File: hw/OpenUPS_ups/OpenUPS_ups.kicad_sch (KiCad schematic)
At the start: 1 part

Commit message: More cleanups and stuff
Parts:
- removed U?: ATtiny204-SS, Package_SO:SOIC-14_3.9x8.7mm_P1.27mm, symbol MCU_Microchip_ATtiny:ATtiny204-SS
- added C706 (x2): 100n 10V, Capacitor_SMD:C_0603_1608Metric, symbol Device:C_Small
- added U101: AVR32DB28x-xSO, Package_SO:SOIC-28W_7.5x17.9mm_P1.27mm, symbol MCU_Microchip_AVR_Dx:AVR32DB28x-xSO
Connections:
- net GND: now also C706.2, C706.2, U101.15 (AGND), U101.21 (GND)
- new net +3V3: C706.1, C706.1, U101.14 (AVDD), U101.20 (VDD), U101.6 (VDDIO2)
- new net I2C_E_SCL: U101.5 (PC3)
- new net I2C_E_SDA: U101.4 (PC2)
- new net I2C_I_SCL: U101.25 (PA3)
- new net I2C_I_SDA: U101.24 (PA2)
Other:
- added sheet Adj_Buck_Boost (12V_Buck_Boost.kicad_sch)
- sheet 12V Buck_Boost ports: added CLIND, CS1, CS2, EN, INT, SCL, SDA, Vin, Vout; removed none
- sheet 5V Buck ports: added EN; removed none
- note added: "Battery terminal goes here"
- note added: "Compatible with any 28-pin SOIC DA, DB or DD device"
- note added: "I2C Ma SCL"
- note added: "I2C Ma SDA"
- note added: "I2C Sl SCL"
- note added: "I2C Sl SDA"

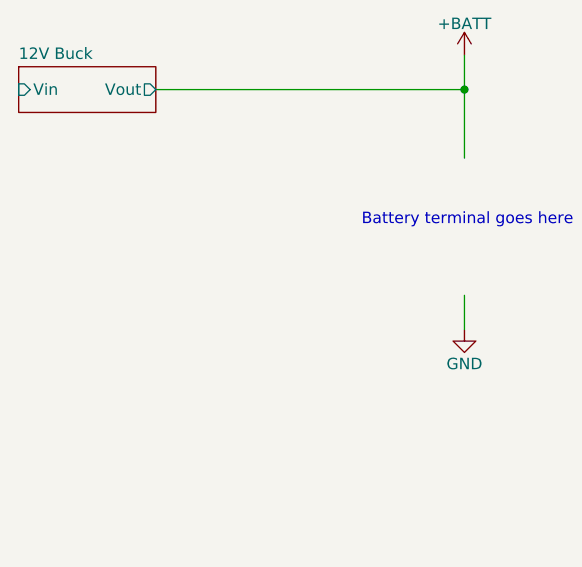
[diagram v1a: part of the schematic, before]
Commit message: Preliminary battery charger circuit
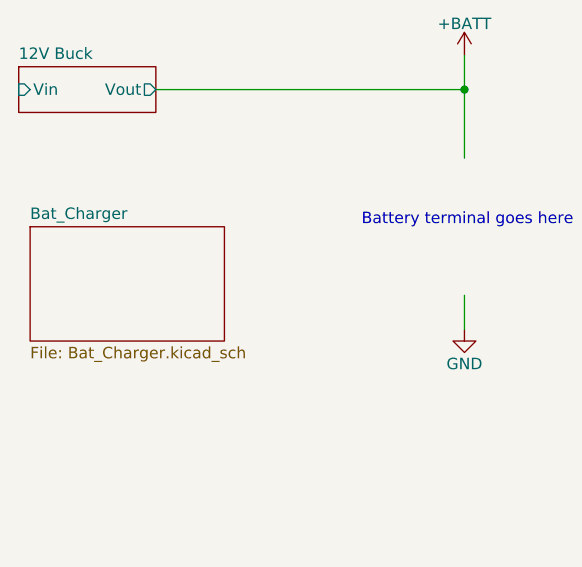
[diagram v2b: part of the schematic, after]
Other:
- added sheet Bat_Charger (Bat_Charger.kicad_sch)
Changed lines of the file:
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@@
+    )
+  )
+  (sheet (at 52.07 62.23) (size 21.59 12.7) (fields_autoplaced)
+    (stroke (width 0.1524) (type solid))
+    (fill (color 0 0 0 0.0000))
+    (property "Sheetname" "Bat_Charger" (at 52.07 61.5184 0)
+      (effects (font (size 1.27 1.27)) (justify left bottom))
+    )
+    (property "Sheetfile" "Bat_Charger.kicad_sch" (at 52.07 75.5146 0)
+      (effects (font (size 1.27 1.27)) (justify left top))
+    )
+    (instances
+      (project "OpenUPS_ups"
+        (path "/f77faec3-eac4-47f3-a2de-ec4a039f4502" (page "6"))
+      )
     )
   )

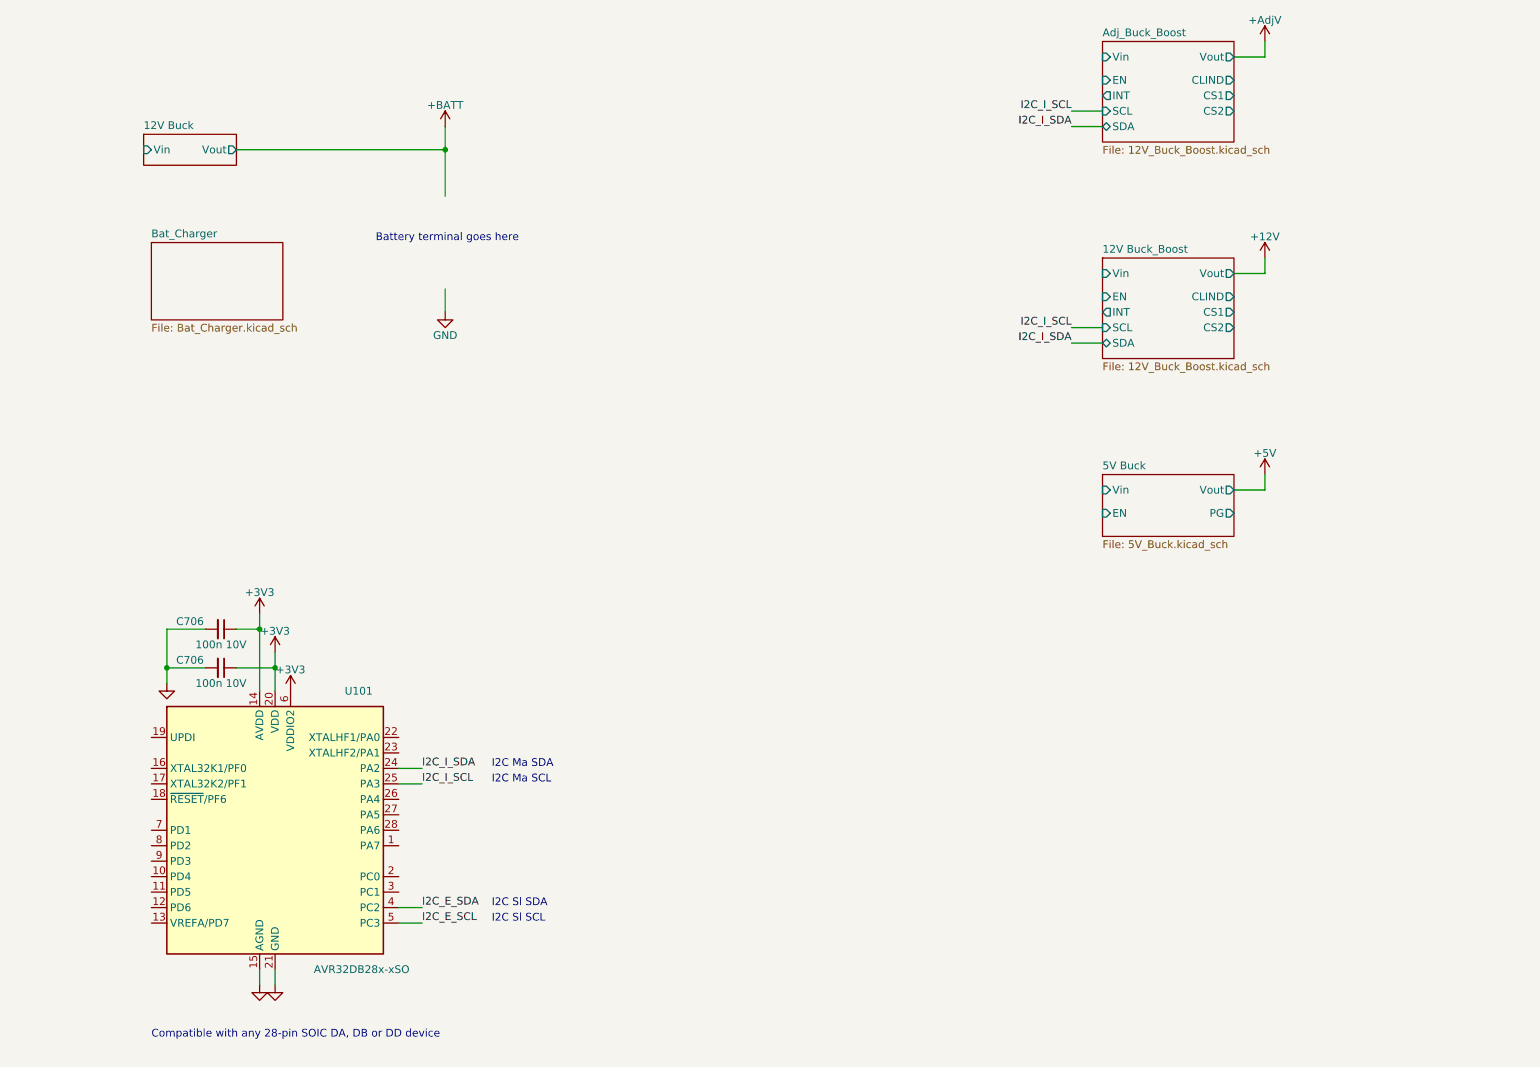
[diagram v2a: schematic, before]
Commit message: Secondary blocks design
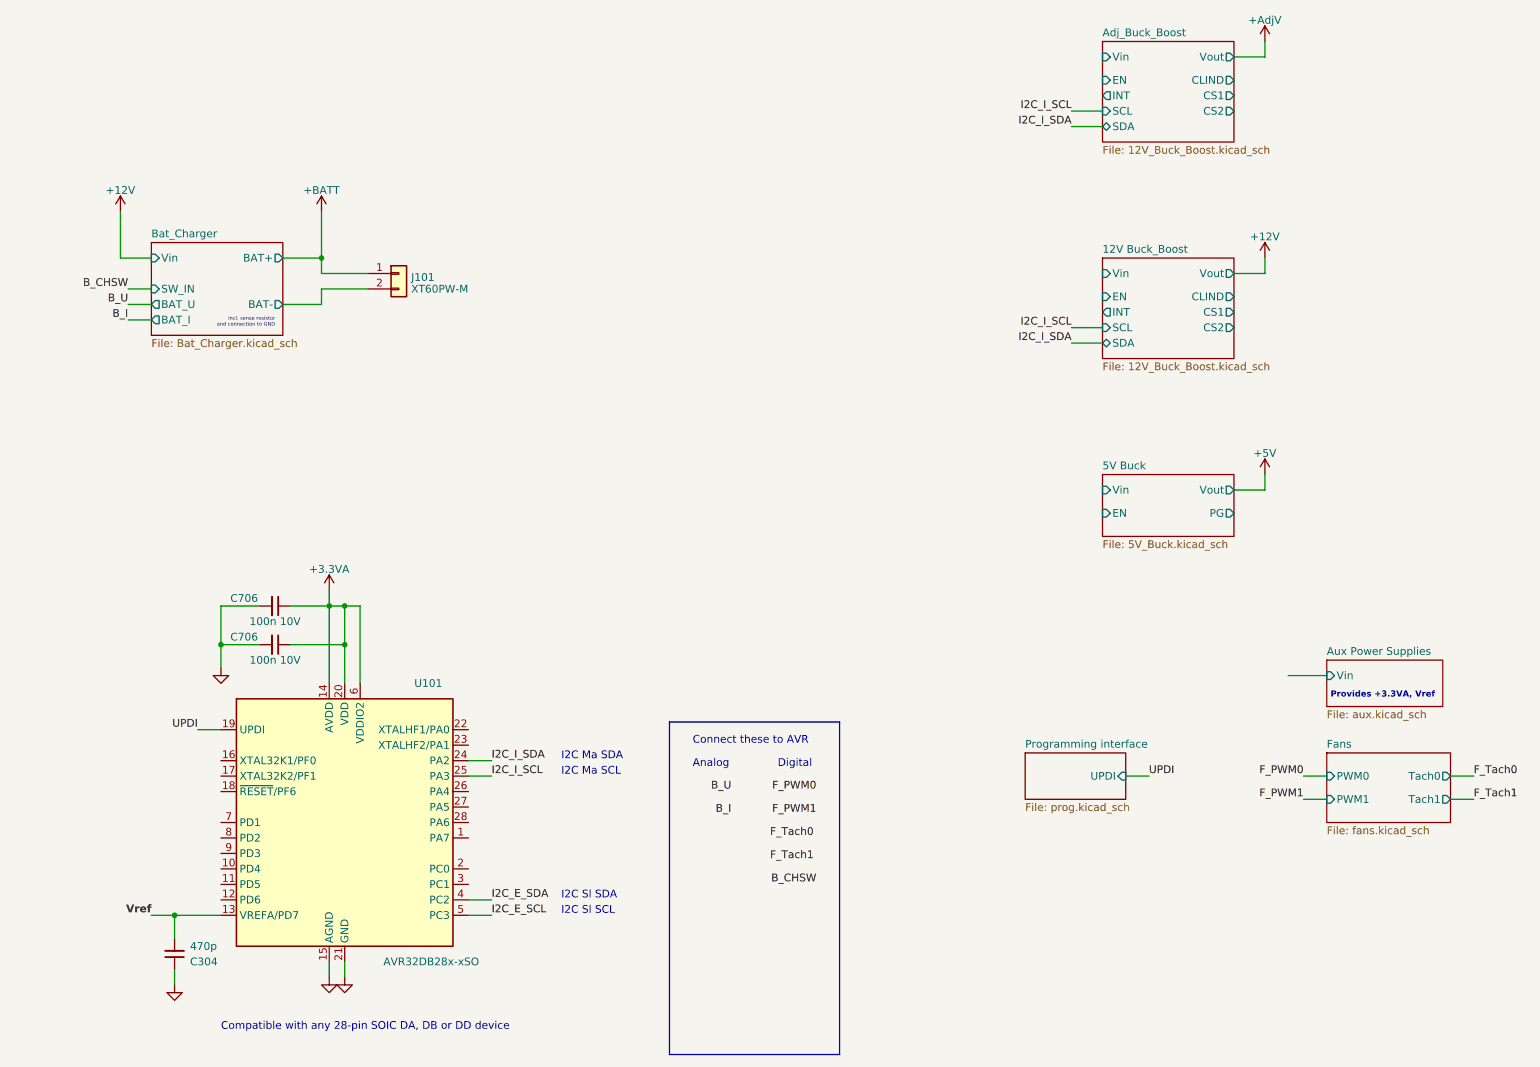
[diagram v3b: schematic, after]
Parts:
- added C304: 470p, Capacitor_SMD:C_0603_1608Metric, symbol Device:C_Small
- added J101: XT60PW-M, Connector_AMASS:AMASS_XT60PW-M_1x02_P7.20mm_Horizontal, symbol Connector_Generic:Conn_01x02
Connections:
- net +BATT: now also J101.1 (Pin_1)
- net GND: now also C304.1
- net Vref: now reaches U101.13 (VREFA/PD7)
- net Vref: now also C304.2
- net UPDI: now reaches U101.19 (UPDI)
- net +3V3 renamed +3.3VA
- new net Bat_Charger/BAT-: J101.2 (Pin_2)
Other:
- removed sheet 12V Buck
- added sheet Aux Power Supplies (aux.kicad_sch)
- added sheet Fans (fans.kicad_sch)
- added sheet Programming interface (prog.kicad_sch)
- sheet Bat_Charger ports: added BAT+, BAT-, BAT_I, BAT_U, SW_IN, Vin; removed none
- note added: "Analog"
- note added: "Connect these to AVR"
- note added: "Digital"
- note added: "Provides +3.3VA, Vref"
- note added: "incl. sense resistor and connection to GND"
- note removed: "Battery terminal goes here"
- moved on the sheet: C706, U101

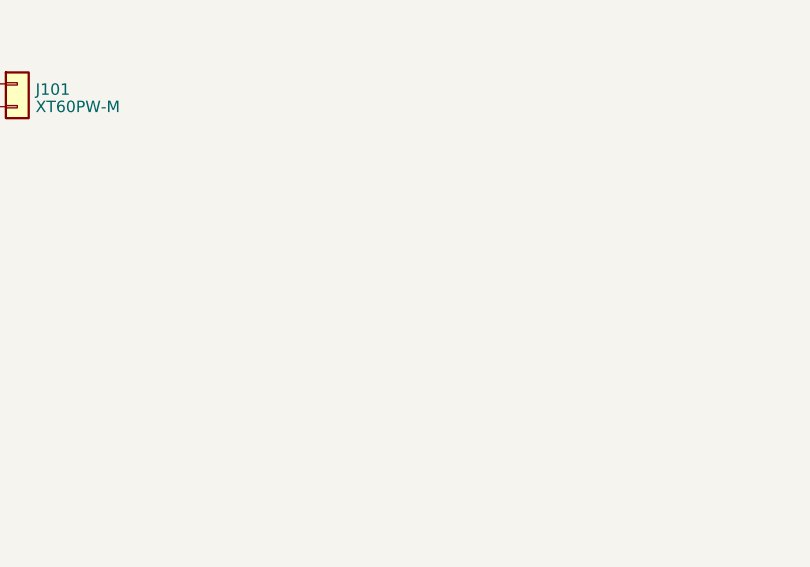
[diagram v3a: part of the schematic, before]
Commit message: Added Ideal Diode ORing solution
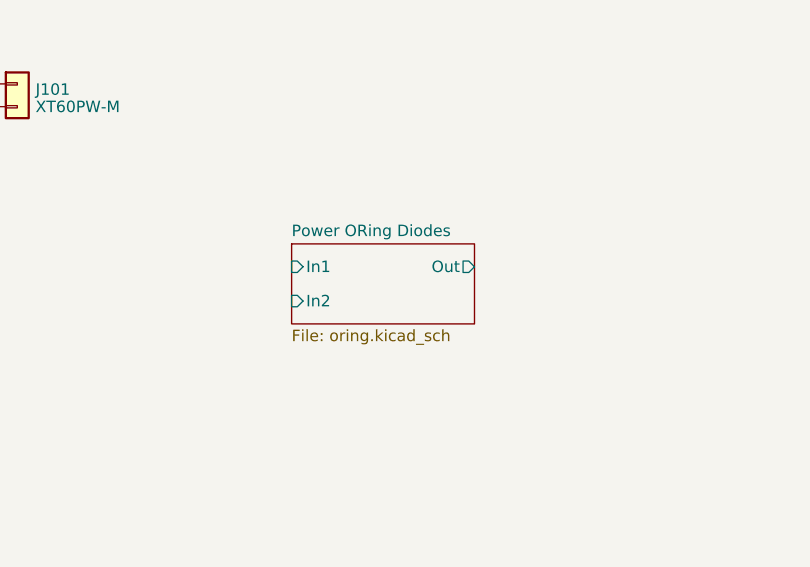
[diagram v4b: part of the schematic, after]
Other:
- added sheet Power ORing Diodes (oring.kicad_sch)
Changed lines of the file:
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@@
+    )
+  )
+  (sheet (at 123.19 85.09) (size 20.32 8.89) (fields_autoplaced)
+    (stroke (width 0.1524) (type solid))
+    (fill (color 0 0 0 0.0000))
+    (property "Sheetname" "Power ORing Diodes" (at 123.19 84.3784 0)
+      (effects (font (size 1.27 1.27)) (justify left bottom))
+    )
+    (property "Sheetfile" "oring.kicad_sch" (at 123.19 94.5646 0)
+      (effects (font (size 1.27 1.27)) (justify left top))
+    )
+    (pin "In1" input (at 123.19 87.63 180)
+      (effects (font (size 1.27 1.27)) (justify left))
+    )
+    (pin "Out" output (at 143.51 87.63 0)
+      (effects (font (size 1.27 1.27)) (justify right))
+    )
+    (pin "In2" input (at 123.19 91.44 180)
+      (effects (font (size 1.27 1.27)) (justify left))
+    )
+    (instances
+      (project "OpenUPS_ups"
+        (path "/f77faec3-eac4-47f3-a2de-ec4a039f4502" (page "9"))
+      )
     )
   )
